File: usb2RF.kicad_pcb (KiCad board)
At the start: 4 copper layers, 40 x 15 mm, 38 parts, among them J1 USB_B_Micro, J2 SMA, J3 ARM 10Pin, U1 nRF24L01P, U2 XC6206P332MR, U3 USBLC6-2SC6, U4 STM32L432KBU6, Y1 16MHz

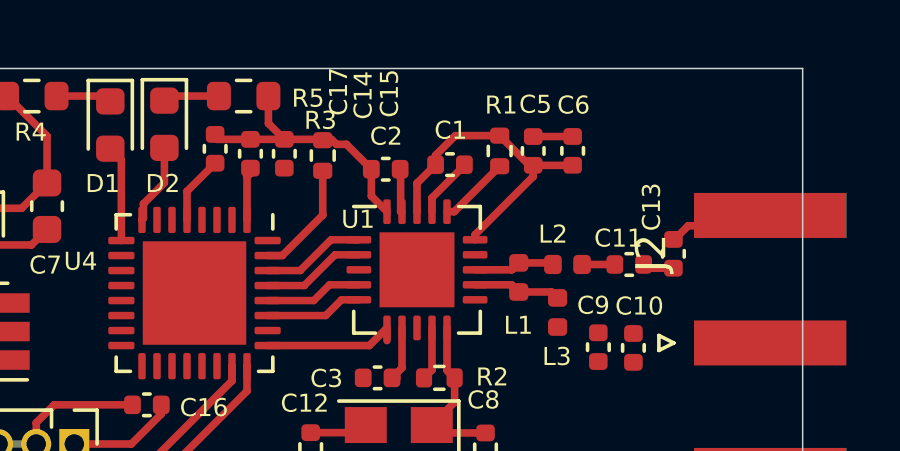
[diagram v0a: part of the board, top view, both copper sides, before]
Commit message: [footprint] update for decoupling capacitor for NRF24L01
Signed-off-by: EasonLiang <liangyx25@163.com>
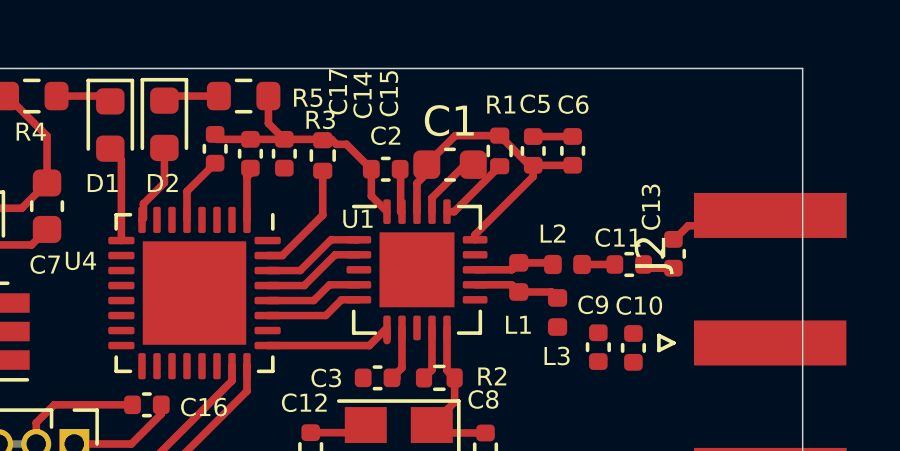
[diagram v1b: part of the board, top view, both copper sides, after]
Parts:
- C1: footprint Capacitor_SMD:C_0402_1005Metric -> Capacitor_SMD:C_0603_1608Metric

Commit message: [relayout]
Signed-off-by: EasonLiang <liangyx25@163.com>
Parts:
- moved C5 2.98 mm to (68.1, 43.0)
- moved J2 2.45 mm to (80.5, 47.3)
- moved C18 2.09 mm to (47.0, 53.9), turned to 180 degrees
- moved C1 2.04 mm to (66.3, 42.5), turned to 90 degrees
- moved C16 1.78 mm to (56.8, 52.4)
- moved U3 1.66 mm to (50.9, 48.8)
- moved C6 1.59 mm to (70.8, 43.0)
- moved J3 1.39 mm to (54.3, 52.6)
- moved C2 1.29 mm to (64.8, 43.1), turned to 90 degrees
- moved U4 1.14 mm to (58.9, 48.3)
- moved R4 1.04 mm to (53.4, 41.5)
- moved FB1 1.01 mm to (48.5, 41.6)
- moved U1 0.95 mm to (66.2, 47.0)
- moved D1 0.94 mm to (56.1, 42.2)
- moved R2 0.94 mm to (67.0, 50.3)
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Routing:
- net GND: track 40.5 -> 4.51 mm
- net +3V3: track 22.5 -> 0.43 mm
- net +5V: track 15.9 -> 0.00 mm, vias 2 -> 0
- net SWCLK: track 9.80 -> 0.00 mm
- net SWDIO: track 7.19 -> 0.00 mm
- net Net-(C4-Pad1): track 6.21 -> 0.19 mm
- net USB_CONN_D+: track 5.09 -> 0.00 mm
- net USB_CONN_D-: track 5.06 -> 0.00 mm
- net NRF_IRQ: track 4.64 -> 0.00 mm
- net Net-(R3-Pad1): track 3.87 -> 0.00 mm
- net NRF_XC1: track 5.74 -> 1.95 mm
- net SPI3_ICS: track 3.47 -> 0.00 mm
- net NRF_CE: track 3.47 -> 0.10 mm
- net Net-(F1-Pad1): track 3.29 -> 0.00 mm
- net SPI3_MISO: track 3.26 -> 0.00 mm
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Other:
- outline, holes or cut-outs redrawn

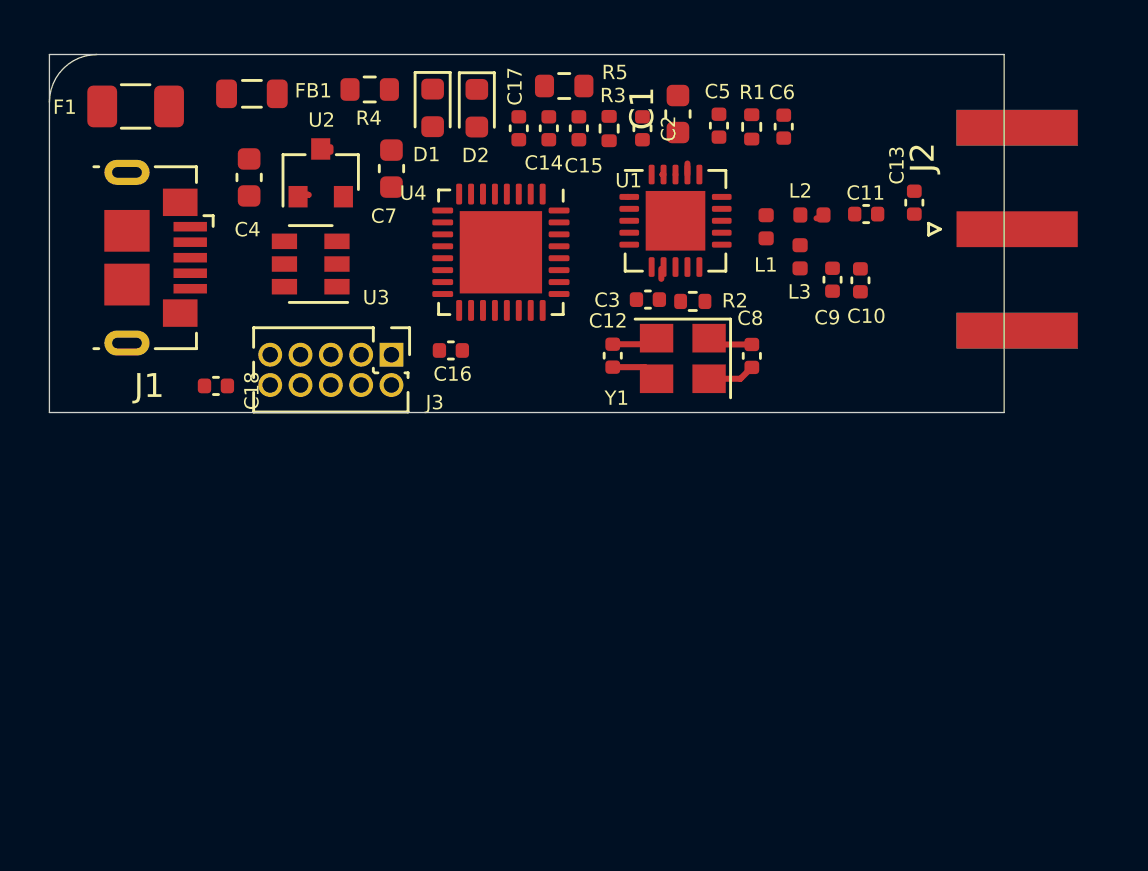
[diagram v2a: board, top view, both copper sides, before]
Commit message: [outline] to 44*15mm
Signed-off-by: EasonLiang <liangyx25@163.com>
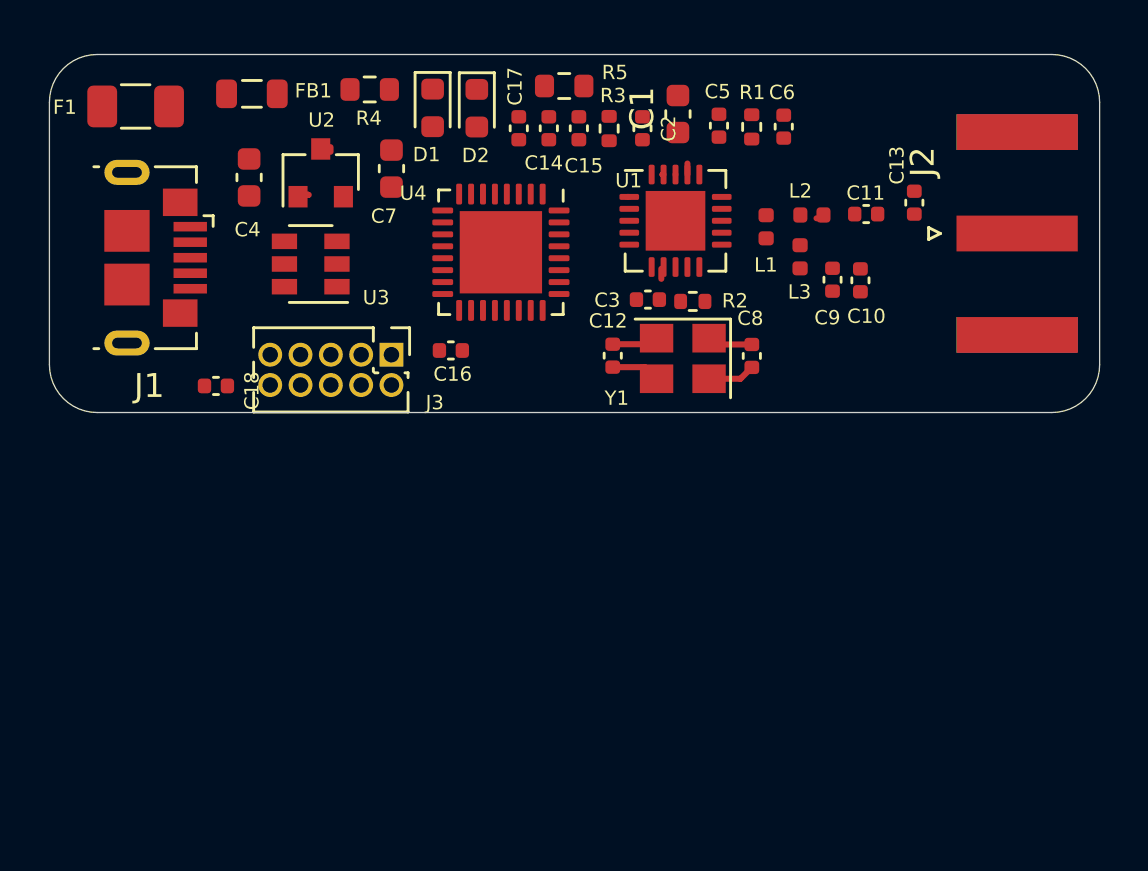
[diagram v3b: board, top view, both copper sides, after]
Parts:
- moved J2 0.18 mm to (80.5, 47.5)
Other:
- board size 40 x 15 mm -> 44 x 15 mm
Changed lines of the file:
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@@
   (general
     (thickness 1.6)
-    (drawings 5)
+    (drawings 8)
     (tracks 22)
     (zones 0)
@@
   )
   (module pcbEsLib:SMA_EdgeMount (layer F.Cu)
-    (at 80.5434 47.3202)
+    (at 80.5434 47.5)
     (descr http://www.amphenolrf.com/132289.html)
     (tags SMA)
@@
     )
   )
+  (gr_arc (start 82 53) (end 84 53) (angle 90) (layer Edge.Cuts) (width 0.05))
+  (gr_arc (start 42 53) (end 42 55) (angle 90) (layer Edge.Cuts) (width 0.05))
+  (gr_arc (start 82 42) (end 82 40) (angle 90) (layer Edge.Cuts) (width 0.05))
   (gr_arc (start 42 42) (end 40 42) (angle 90) (layer Edge.Cuts) (width 0.05))
-  (gr_line (start 40 40) (end 40 55) (layer Edge.Cuts) (width 0.05))
-  (gr_line (start 40 55) (end 80 55) (layer Edge.Cuts) (width 0.05))
-  (gr_line (start 80 40) (end 80 55) (layer Edge.Cuts) (width 0.05))
-  (gr_line (start 40 40) (end 80 40) (layer Edge.Cuts) (width 0.05))
+  (gr_line (start 40 42) (end 40 53) (layer Edge.Cuts) (width 0.05))
+  (gr_line (start 42 55) (end 82 55) (layer Edge.Cuts) (width 0.05))
+  (gr_line (start 84 42) (end 84 53) (layer Edge.Cuts) (width 0.05))
+  (gr_line (start 42 40) (end 82 40) (layer Edge.Cuts) (width 0.05))
   (segment (start 68.95168 53.58548) (end 69.42836 53.1088) (width 0.254) (layer F.Cu) (net 1))
   (segment (start 67.63784 53.58548) (end 68.95168 53.58548) (width 0.254) (layer F.Cu) (net 1))

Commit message: [route] left part
Signed-off-by: EasonLiang <liangyx25@163.com>
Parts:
- moved C16 0.97 mm to (56.6, 53.3)
- moved J3 0.92 mm to (53.4, 52.5)
- moved C18 0.90 mm to (46.1, 53.9)
- moved U4 0.77 mm to (58.2, 47.9)
- moved C3 0.70 mm to (64.4, 50.3)
- moved R2 0.48 mm to (67.4, 50.3)
- moved C7 0.45 mm to (53.9, 44.6)
- moved C4 0.43 mm to (48.3, 44.7)
- moved U3 0.43 mm to (50.9, 48.3)
- moved U2 0.43 mm to (51.3, 44.5)
- moved C1 0.21 mm to (66.4, 42.3)
- moved C5 0.16 mm to (68.0, 42.8)
- moved J1 0.08 mm to (44.5, 48.4)
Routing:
- net GND: track 4.51 -> 88.7 mm, vias 0 -> 8
- net +3V3: track 0.43 -> 52.6 mm, vias 0 -> 6
- net nRST: track 0.00 -> 20.5 mm, vias 0 -> 1
- net Net-(J1-Pad6): track 0.00 -> 13.3 mm
- net +5V: track 0.00 -> 13.0 mm, vias 0 -> 2
- net SWCLK: track 0.00 -> 11.6 mm
- net USB_D-: track 0.00 -> 10.2 mm
- net USB_D+: track 0.00 -> 9.92 mm
- net SWDIO: track 0.00 -> 9.40 mm
- net Net-(C11-Pad1): track 0.00 -> 6.18 mm
- net Net-(C4-Pad1): track 0.19 -> 5.89 mm
- net SPI3_SCK: track 0.00 -> 5.66 mm, vias 0 -> 2
- net SPI3_MISO: track 0.00 -> 4.77 mm
- net Net-(R3-Pad1): track 0.00 -> 4.61 mm
- net SPI3_MOSI: track 0.00 -> 4.37 mm
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
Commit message: [route] all
Signed-off-by: EasonLiang <liangyx25@163.com>
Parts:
- moved C12 3.97 mm to (67.4, 53.6), turned to 315 degrees
- moved C8 3.48 mm to (71.1, 49.6), turned to 315 degrees
- moved Y1 3.04 mm to (69.4, 51.8), turned to 225 degrees
- moved C10 1.30 mm to (75.3, 49.4)
- moved C9 1.30 mm to (74.1, 49.4)
- moved L3 1.30 mm to (72.7, 48.5)
- moved C3 0.81 mm to (64.9, 50.9), turned to 225 degrees
- moved R2 0.57 mm to (67.1, 50.8), turned to 45 degrees
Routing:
- net GND: track 88.7 -> 168.1 mm, vias 8 -> 11
- net +3V3: track 52.6 -> 65.0 mm, vias 6 -> 7
- net NRF_VDD_PA: track 0.00 -> 7.51 mm
- net NRF_IRQ: track 0.00 -> 5.34 mm
- net NRF_ANT1: track 0.00 -> 4.78 mm
- net NRF_XC2: track 3.56 -> 6.76 mm
- net Net-(D2-Pad2): track 2.92 -> 4.97 mm
- net NRF_XC1: track 4.36 -> 5.66 mm
- net SPI3_SCK: track 5.66 -> 6.22 mm

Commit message: [DRC]
Signed-off-by: EasonLiang <liangyx25@163.com>
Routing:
- net GND: track 168.1 -> 172.7 mm, vias 11 -> 12
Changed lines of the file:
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@@
     (thickness 1.6)
     (drawings 8)
-    (tracks 371)
+    (tracks 378)
     (zones 0)
     (modules 38)
@@
   (segment (start 66.5864 41.7322) (end 66.3702 41.516) (width 0.254) (layer F.Cu) (net 1))
   (segment (start 67.3608 41.7322) (end 66.5864 41.7322) (width 0.254) (layer F.Cu) (net 1))
-  (segment (start 67.973 42.3444) (end 67.3608 41.7322) (width 0.254) (layer F.Cu) (net 1))
+  (segment (start 67.973 42.3444) (end 67.4243 41.7957) (width 0.254) (layer F.Cu) (net 1))
   (segment (start 68.0466 42.3444) (end 67.973 42.3444) (width 0.254) (layer F.Cu) (net 1))
   (segment (start 63.9064 40.7924) (end 63.373 41.3258) (width 0.254) (layer F.Cu) (net 1))
@@
   (segment (start 54.8767 49.5681) (end 54.5211 49.5681) (width 0.254) (layer B.Cu) (net 1))
   (via (at 54.6862 49.2506) (size 0.8) (drill 0.4) (layers F.Cu B.Cu) (net 1))
-  (segment (start 61.468 45.1866) (end 57.404 49.2506) (width 0.254) (layer B.Cu) (net 1))
   (segment (start 57.404 49.2506) (end 54.6862 49.2506) (width 0.254) (layer B.Cu) (net 1))
   (segment (start 55.792 49.6925) (end 55.1281 49.6925) (width 0.254) (layer F.Cu) (net 1))
@@
   (segment (start 58.983744 44.438536) (end 58.983744 44.378744) (width 0.254) (layer B.Cu) (net 3))
   (segment (start 56.55289 44.39189) (end 57.90692 43.03786) (width 0.254) (layer F.Cu) (net 4))
-  (segment (start 55.8174 43.26302) (end 56.05526 43.02516) (width 0.254) (layer F.Cu) (net 5))
-  (segment (start 55.8174 46.0655) (end 55.8174 43.26302) (width 0.254) (layer F.Cu) (net 5))
   (segment (start 53.7972 48.38764) (end 52.80592 47.39636) (width 0.254) (layer F.Cu) (net 6))
   (segment (start 53.7972 49.649932) (end 53.7972 48.38764) (width 0.254) (layer F.Cu) (net 6))
@@
   (segment (start 50.049199 51.674799) (end 49.163201 51.674799) (width 0.254) (layer F.Cu) (net 1))
   (segment (start 50.8762 52.5018) (end 50.049199 51.674799) (width 0.254) (layer F.Cu) (net 1))
+  (segment (start 67.4243 41.7957) (end 67.3608 41.7322) (width 0.254) (layer F.Cu) (net 1))
+  (via (at 67.4243 41.7957) (size 0.8) (drill 0.4) (layers F.Cu B.Cu) (net 1))
+  (segment (start 67.2338 41.9862) (end 67.2338 43.9962) (width 0.254) (layer B.Cu) (net 1))
+  (segment (start 67.4243 41.7957) (end 67.2338 41.9862) (width 0.254) (layer B.Cu) (net 1))
+  (segment (start 57.5564 49.0982) (end 57.4675 49.1871) (width 0.254) (layer B.Cu) (net 1))
+  (segment (start 57.4675 49.1871) (end 57.404 49.2506) (width 0.254) (layer B.Cu) (net 1))
+  (segment (start 57.5564 46.9138) (end 57.5564 49.0982) (width 0.254) (layer B.Cu) (net 1))
+  (segment (start 61.468 45.1866) (end 57.4675 49.1871) (width 0.254) (layer B.Cu) (net 1))
   (segment (start 70.508918 43.50252) (end 70.7644 43.50252) (width 0.254) (layer F.Cu) (net 2))
   (segment (start 68.168 45.843438) (end 70.508918 43.50252) (width 0.254) (layer F.Cu) (net 2))
@@
   (segment (start 56.4795 44.46528) (end 57.90692 43.03786) (width 0.254) (layer F.Cu) (net 4))
   (segment (start 56.4795 45.505) (end 56.4795 44.46528) (width 0.254) (layer F.Cu) (net 4))
+  (segment (start 55.792 43.28842) (end 56.05526 43.02516) (width 0.254) (layer F.Cu) (net 5))
+  (segment (start 55.792 46.1925) (end 55.792 43.28842) (width 0.254) (layer F.Cu) (net 5))
   (segment (start 58.819266 54.598801) (end 59.9795 53.438567) (width 0.254) (layer F.Cu) (net 9))
   (segment (start 52.973201 54.598801) (end 58.819266 54.598801) (width 0.254) (layer F.Cu) (net 9))

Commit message: [anneta]
Signed-off-by: EasonLiang <liangyx25@163.com>
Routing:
- net GND: track 172.7 -> 191.2 mm, vias 12 -> 23

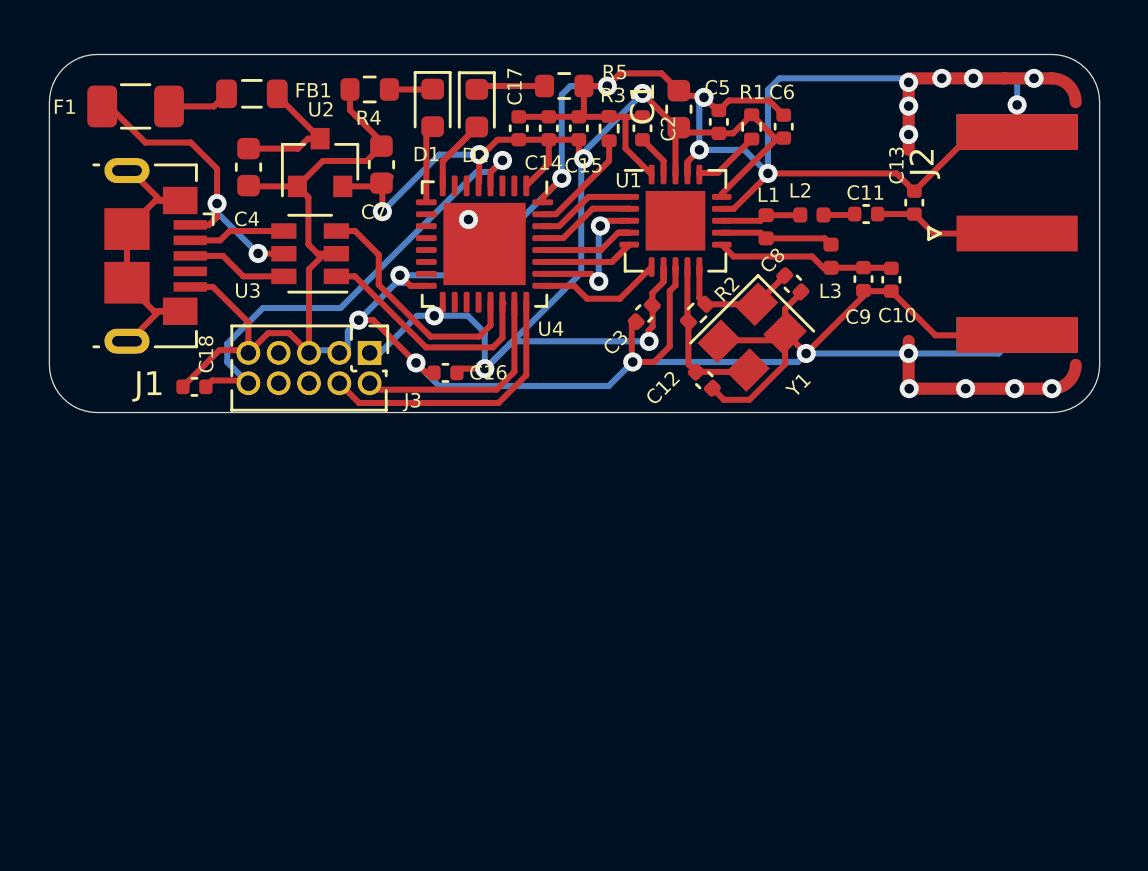
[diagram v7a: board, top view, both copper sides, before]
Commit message: [joint panel] joint panel with anchor holes
Signed-off-by: EasonLiang <liangyx25@163.com>
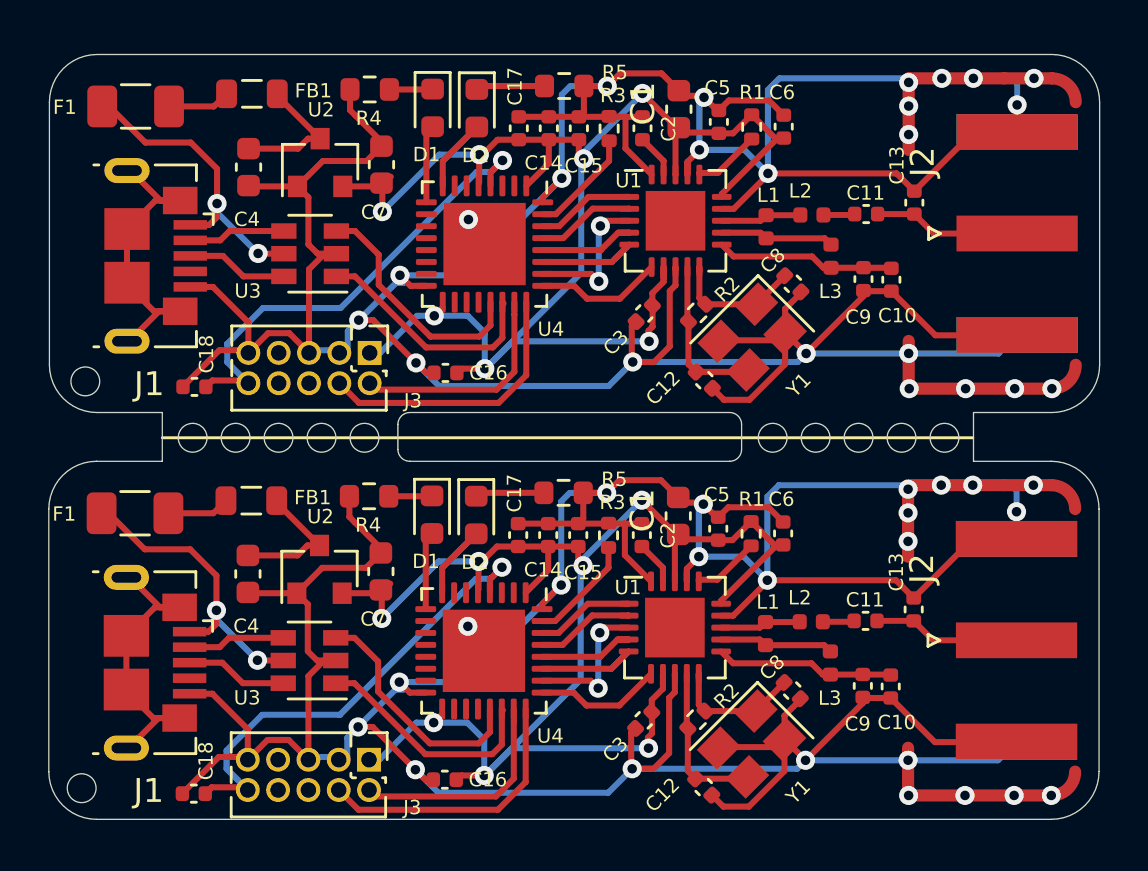
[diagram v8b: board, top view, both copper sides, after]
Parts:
- added C1: 10uF, Capacitor_SMD:C_0603_1608Metric, F.Cu at (66.3, 59.3)
- added C10: 4p7, Capacitor_SMD:C_0402_1005Metric, F.Cu at (75.2, 66.5)
- added C11: 1p5, Capacitor_SMD:C_0402_1005Metric, F.Cu at (74.2, 63.7)
- added C12: 12pF, Capacitor_SMD:C_0402_1005Metric, F.Cu at (67.4, 70.7)
- added C13: 1p, Capacitor_SMD:C_0402_1005Metric, F.Cu at (76.2, 63.3)
- added C14: 1uF, Capacitor_SMD:C_0402_1005Metric, F.Cu at (60.9, 60.1)
- added C15: 100nF, Capacitor_SMD:C_0402_1005Metric, F.Cu at (62.2, 60.1)
- added C16: 100nF, Capacitor_SMD:C_0402_1005Metric, F.Cu at (56.6, 70.4)
- added C17: 100nF, Capacitor_SMD:C_0402_1005Metric, F.Cu at (59.6, 60.1)
- added C18: 100nF, Capacitor_SMD:C_0402_1005Metric, F.Cu at (46.1, 71.0)
- added C2: 10nF, Capacitor_SMD:C_0402_1005Metric, F.Cu at (64.8, 60.1)
- added C3: 10nF, Capacitor_SMD:C_0402_1005Metric, F.Cu at (64.9, 67.9)
- added C4: 10uF, Capacitor_SMD:C_0603_1608Metric, F.Cu at (48.3, 61.8)
- added C5: 10nF, Capacitor_SMD:C_0402_1005Metric, F.Cu at (68.0, 59.9)
- added C6: 10nF, Capacitor_SMD:C_0402_1005Metric, F.Cu at (70.7, 60.1)
- added C7: 10uF, Capacitor_SMD:C_0603_1608Metric, F.Cu at (53.9, 61.7)
- added C8: 12pF, Capacitor_SMD:C_0402_1005Metric, F.Cu at (71.1, 66.6)
- added C9: 2n2, Capacitor_SMD:C_0402_1005Metric, F.Cu at (74.1, 66.5)
- added D1: Green, LED_SMD:LED_0603_1608Metric, F.Cu at (56.0, 59.3)
- added D2: Blue, LED_SMD:LED_0603_1608Metric, F.Cu at (57.9, 59.3)
- added F1: 100mA, Fuse:Fuse_1206_3216Metric, F.Cu at (43.6, 59.2)
- added FB1: 100MHz, Inductor_SMD:L_0805_2012Metric, F.Cu at (48.5, 58.7)
- added J1: USB_B_Micro, pcbEsLib:USB-Micro, F.Cu at (44.4, 65.5)
- added J2: SMA, pcbEsLib:SMA_EdgeMount, F.Cu at (80.5, 64.5)
- added J3: ARM 10Pin, Connector_PinHeader_1.27mm:PinHeader_2x05_P1.27mm_Vertical, F.Cu at (53.4, 69.5)
- added L1: 8n2, Inductor_SMD:L_0402_1005Metric, F.Cu at (70.0, 64.3)
- added L2: 3n9, Inductor_SMD:L_0402_1005Metric, F.Cu at (71.9, 63.8)
- added L3: 2n7, Inductor_SMD:L_0402_1005Metric, F.Cu at (72.7, 65.5)
- added R1: 22K, Resistor_SMD:R_0402_1005Metric, F.Cu at (69.4, 60.1)
- added R2: 1M, Resistor_SMD:R_0402_1005Metric, F.Cu at (67.1, 67.9)
- added R3: 10K, Resistor_SMD:R_0402_1005Metric, F.Cu at (63.4, 60.1)
- added R4: 2K2, Resistor_SMD:R_0603_1608Metric, F.Cu at (53.4, 58.5)
- added R5: 2K2, Resistor_SMD:R_0603_1608Metric, F.Cu at (61.5, 58.4)
- added U1: nRF24L01P, Package_DFN_QFN:QFN-20-1EP_4x4mm_P0.5mm_EP2.5x2.5mm, F.Cu at (66.2, 64.0)
- added U2: XC6206P332MR, Package_TO_SOT_SMD:SOT-23, F.Cu at (51.3, 61.6)
- added U3: USBLC6-2SC6, Package_TO_SOT_SMD:SOT-23-6, F.Cu at (50.9, 65.4)
- added U4: STM32L432KBU6, Package_DFN_QFN:QFN-32-1EP_5x5mm_P0.5mm_EP3.45x3.45mm, F.Cu at (58.2, 65.0)
- added Y1: 16MHz, Crystal:Crystal_SMD_3225-4Pin_3.2x2.5mm, F.Cu at (69.4, 68.9)
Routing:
- net (no net): track 0.00 -> 448.3 mm, vias 0 -> 35
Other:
- board size 44 x 15 mm -> 44 x 32 mm
